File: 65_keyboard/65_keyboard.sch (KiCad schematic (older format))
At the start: 10 parts, among them SW0-0 MX, SW1-0 MX, SW2-0 MX, SW3-0 MX, SW4-0 MX

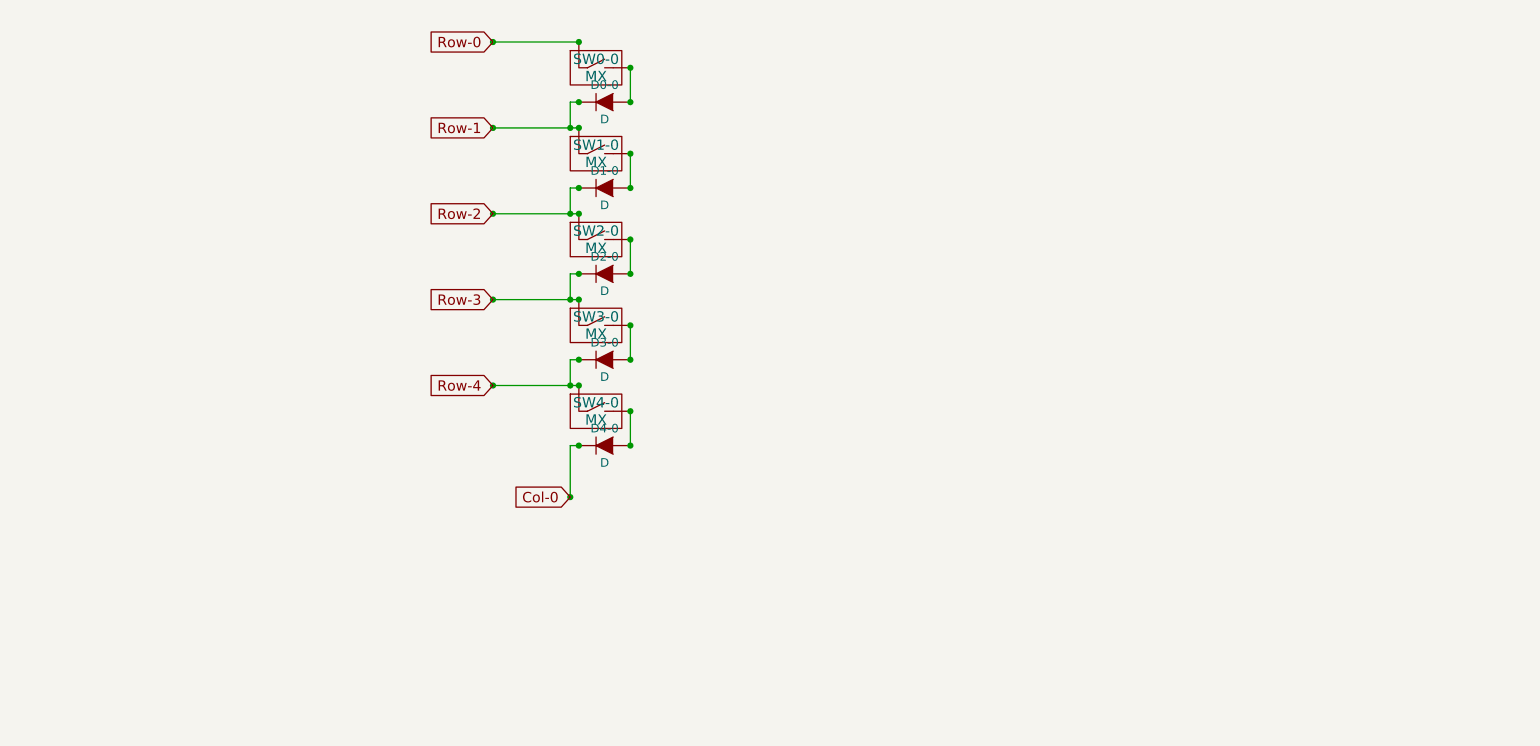
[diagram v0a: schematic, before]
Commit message: Adds all keys to keyboard, and places them on the PCB
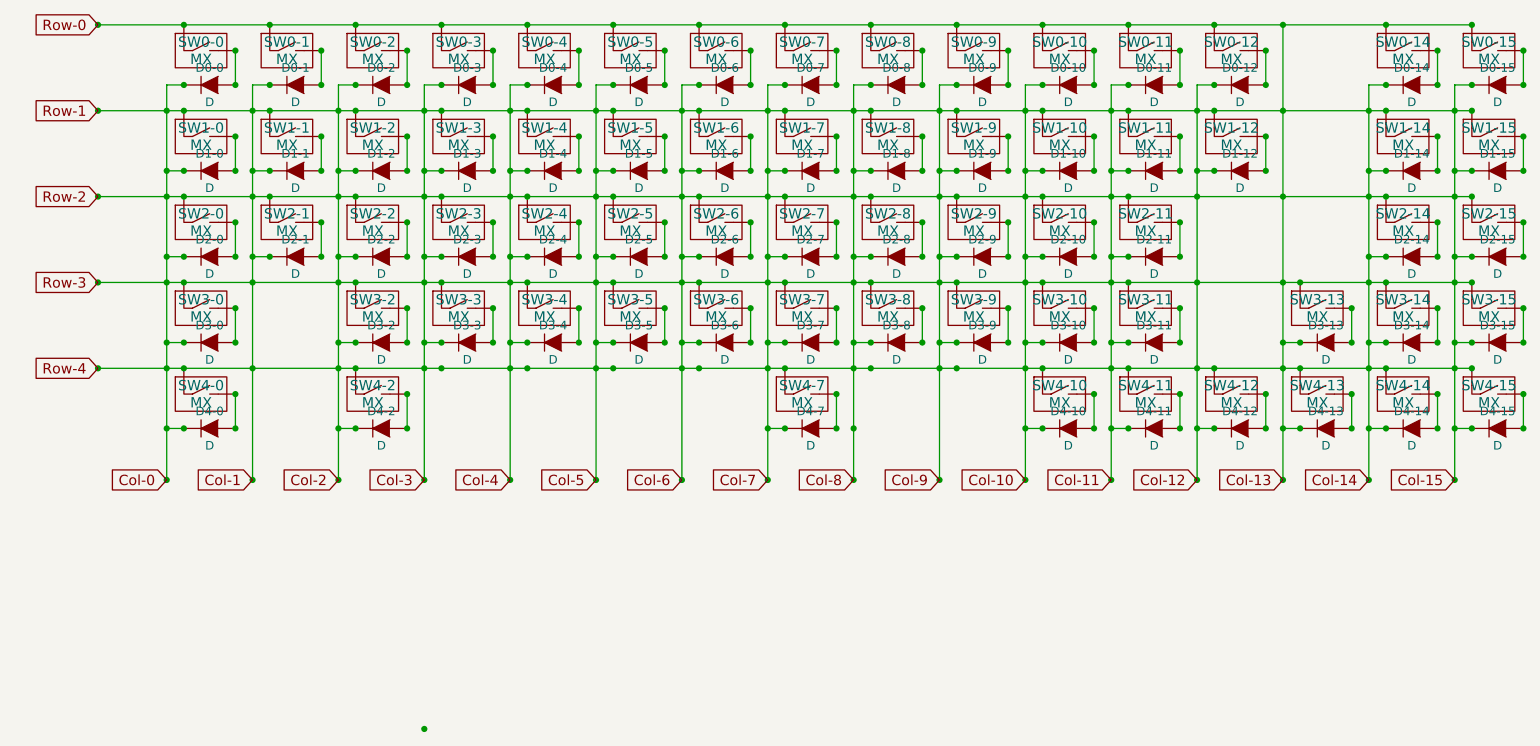
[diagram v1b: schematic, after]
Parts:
- added D0-1, D0-10, D0-11, D0-12, D0-14, D0-15, D0-2, D0-3, D0-4, D0-5, D0-6, D0-7, D0-8, D0-9, D1-1, D1-10, D1-11, D1-12, D1-14, D1-15, D1-2, D1-3, D1-4, D1-5, D1-6, D1-7, D1-8, D1-9, D2-1, D2-10, D2-11, D2-14, D2-15, D2-2, D2-3, D2-4, D2-5, D2-6, D2-7, D2-8, D2-9, D3-10, D3-11, D3-13, D3-14, D3-15, D3-2, D3-3, D3-4, D3-5, D3-6, D3-7, D3-8, D3-9, D4-10, D4-11, D4-12, D4-13, D4-14, D4-15, D4-2, D4-7: D, Diodes_ThroughHole:Diode_DO-35_SOD27_Horizontal_RM10, symbol D
- added SW0-1, SW0-10, SW0-11, SW0-12, SW0-15, SW0-2, SW0-3, SW0-4, SW0-5, SW0-6, SW0-7, SW0-8, SW0-9, SW1-1, SW1-10, SW1-11, SW1-12, SW1-15, SW1-2, SW1-3, SW1-4, SW1-5, SW1-6, SW1-7, SW1-8, SW1-9, SW2-1, SW2-10, SW2-11, SW2-15, SW2-2, SW2-3, SW2-4, SW2-5, SW2-6, SW2-7, SW2-8, SW2-9, SW3-10, SW3-11, SW3-14, SW3-15, SW3-2, SW3-3, SW3-4, SW3-5, SW3-6, SW3-7, SW3-8, SW3-9, SW4-11, SW4-13, SW4-14, SW4-15: MX, Keyboard:CHERRY_PLATE_100H, symbol MX
- added SW0-14: MX, Keyboard:CHERRY_PLATE_200H, symbol MX
- added SW1-14, SW4-2: MX, Keyboard:CHERRY_PLATE_150H, symbol MX
- added SW2-14: MX, Keyboard:CHERRY_PLATE_225H, symbol MX
- added SW3-13: MX, Keyboard:CHERRY_PLATE_175H, symbol MX
- added SW4-10, SW4-12: MX, Keyboard:CHERRY_PLATE_125H, symbol MX
- added SW4-7: MX, Keyboard:CHERRY_PLATE_625H, symbol MX
- SW0-0: footprint Keyboard:CHERRY_PCB_100H -> Keyboard:CHERRY_PLATE_100H
- SW1-0: footprint Keyboard:CHERRY_PCB_150H -> Keyboard:CHERRY_PLATE_150H
- SW2-0: footprint Keyboard:CHERRY_PCB_200H -> Keyboard:CHERRY_PLATE_175H
- SW3-0: footprint Keyboard:CHERRY_PCB_275H -> Keyboard:CHERRY_PLATE_225H
- SW4-0: footprint Keyboard:CHERRY_PLATE_150H -> Keyboard:CHERRY_PLATE_175H
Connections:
- net Row-0 is gone; now on net Col-0: SW0-0.1 (A)
- net Row-1 is gone; now on net Col-0: D0-0.1 (K), SW1-0.1 (A)
- net Row-2 is gone; now on net Col-0: D1-0.1 (K), SW2-0.1 (A)
- net Row-3 is gone; now on net Col-0: D2-0.1 (K), SW3-0.1 (A)
- net Row-4 is gone; now on net Col-0: D3-0.1 (K), SW4-0.1 (A)
- net Col-0: now also D0-1.1 (K), D0-10.1 (K), D0-11.1 (K), D0-12.1 (K), D0-14.1 (K), D0-15.1 (K), D0-2.1 (K), D0-3.1 (K), D0-4.1 (K), D0-5.1 (K), D0-6.1 (K), D0-7.1 (K), D0-8.1 (K), D0-9.1 (K), D1-1.1 (K), D1-10.1 (K), D1-11.1 (K), D1-12.1 (K), D1-14.1 (K), D1-15.1 (K), D1-2.1 (K), D1-3.1 (K), D1-4.1 (K), D1-5.1 (K), D1-6.1 (K), D1-7.1 (K), D1-8.1 (K), D1-9.1 (K), D2-1.1 (K), D2-10.1 (K), D2-11.1 (K), D2-14.1 (K), D2-15.1 (K), D2-2.1 (K), D2-3.1 (K), D2-4.1 (K), D2-5.1 (K), D2-6.1 (K), D2-7.1 (K), D2-8.1 (K), D2-9.1 (K), D3-10.1 (K), D3-11.1 (K), D3-13.1 (K), D3-14.1 (K), D3-15.1 (K), D3-2.1 (K), D3-3.1 (K), D3-4.1 (K), D3-5.1 (K), D3-6.1 (K), D3-7.1 (K), D3-8.1 (K), D3-9.1 (K), D4-10.1 (K), D4-11.1 (K), D4-12.1 (K), D4-13.1 (K), D4-14.1 (K), D4-15.1 (K), D4-2.1 (K), D4-7.1 (K), SW0-1.1 (A), SW0-10.1 (A), SW0-11.1 (A), SW0-12.1 (A), SW0-14.1 (A), SW0-15.1 (A), SW0-2.1 (A), SW0-3.1 (A), SW0-4.1 (A), SW0-5.1 (A), SW0-6.1 (A), SW0-7.1 (A), SW0-8.1 (A), SW0-9.1 (A), SW1-1.1 (A), SW1-10.1 (A), SW1-11.1 (A), SW1-12.1 (A), SW1-14.1 (A), SW1-15.1 (A), SW1-2.1 (A), SW1-3.1 (A), SW1-4.1 (A), SW1-5.1 (A), SW1-6.1 (A), SW1-7.1 (A), SW1-8.1 (A), SW1-9.1 (A), SW2-1.1 (A), SW2-10.1 (A), SW2-11.1 (A), SW2-14.1 (A), SW2-15.1 (A), SW2-2.1 (A), SW2-3.1 (A), SW2-4.1 (A), SW2-5.1 (A), SW2-6.1 (A), SW2-7.1 (A), SW2-8.1 (A), SW2-9.1 (A), SW3-10.1 (A), SW3-11.1 (A), SW3-13.1 (A), SW3-14.1 (A), SW3-15.1 (A), SW3-2.1 (A), SW3-3.1 (A), SW3-4.1 (A), SW3-5.1 (A), SW3-6.1 (A), SW3-7.1 (A), SW3-8.1 (A), SW3-9.1 (A), SW4-10.1 (A), SW4-11.1 (A), SW4-12.1 (A), SW4-13.1 (A), SW4-14.1 (A), SW4-15.1 (A), SW4-2.1 (A), SW4-7.1 (A)
- new net: D0-1.2 (A), SW0-1.2 (B)
- new net: D1-1.2 (A), SW1-1.2 (B)
- new net: D2-1.2 (A), SW2-1.2 (B)
- new net: D0-2.2 (A), SW0-2.2 (B)
- new net: D1-2.2 (A), SW1-2.2 (B)
- new net: D2-2.2 (A), SW2-2.2 (B)
- new net: D3-2.2 (A), SW3-2.2 (B)
- new net: D4-2.2 (A), SW4-2.2 (B)
- new net: D0-3.2 (A), SW0-3.2 (B)
- new net: D1-3.2 (A), SW1-3.2 (B)
- new net: D2-3.2 (A), SW2-3.2 (B)
- new net: D3-3.2 (A), SW3-3.2 (B)
- new net: D0-4.2 (A), SW0-4.2 (B)
- new net: D1-4.2 (A), SW1-4.2 (B)
- new net: D2-4.2 (A), SW2-4.2 (B)
- new net: D3-4.2 (A), SW3-4.2 (B)
- new net: D0-5.2 (A), SW0-5.2 (B)
- new net: D1-5.2 (A), SW1-5.2 (B)
- new net: D2-5.2 (A), SW2-5.2 (B)
- new net: D3-5.2 (A), SW3-5.2 (B)
- new net: D0-6.2 (A), SW0-6.2 (B)
- new net: D1-6.2 (A), SW1-6.2 (B)
- new net: D2-6.2 (A), SW2-6.2 (B)
- new net: D3-6.2 (A), SW3-6.2 (B)
- new net: D0-7.2 (A), SW0-7.2 (B)
- new net: D1-7.2 (A), SW1-7.2 (B)
- new net: D2-7.2 (A), SW2-7.2 (B)
- new net: D3-7.2 (A), SW3-7.2 (B)
- new net: D4-7.2 (A), SW4-7.2 (B)
- new net: D0-8.2 (A), SW0-8.2 (B)
- new net: D1-8.2 (A), SW1-8.2 (B)
- new net: D2-8.2 (A), SW2-8.2 (B)
- new net: D3-8.2 (A), SW3-8.2 (B)
- new net: D0-9.2 (A), SW0-9.2 (B)
- new net: D1-9.2 (A), SW1-9.2 (B)
- new net: D2-9.2 (A), SW2-9.2 (B)
- new net: D3-9.2 (A), SW3-9.2 (B)
- new net: D0-10.2 (A), SW0-10.2 (B)
- new net: D1-10.2 (A), SW1-10.2 (B)
- new net: D2-10.2 (A), SW2-10.2 (B)
- new net: D3-10.2 (A), SW3-10.2 (B)
- new net: D4-10.2 (A), SW4-10.2 (B)
- new net: D0-11.2 (A), SW0-11.2 (B)
- new net: D1-11.2 (A), SW1-11.2 (B)
- new net: D2-11.2 (A), SW2-11.2 (B)
- new net: D3-11.2 (A), SW3-11.2 (B)
- new net: D4-11.2 (A), SW4-11.2 (B)
- new net: D0-12.2 (A), SW0-12.2 (B)
- new net: D1-12.2 (A), SW1-12.2 (B)
- new net: D4-12.2 (A), SW4-12.2 (B)
- new net: D3-13.2 (A), SW3-13.2 (B)
- new net: D4-13.2 (A), SW4-13.2 (B)
- new net: D0-14.2 (A), SW0-14.2 (B)
- new net: D1-14.2 (A), SW1-14.2 (B)
- new net: D2-14.2 (A), SW2-14.2 (B)
- new net: D3-14.2 (A), SW3-14.2 (B)
- new net: D4-14.2 (A), SW4-14.2 (B)
- new net: D0-15.2 (A), SW0-15.2 (B)
- new net: D1-15.2 (A), SW1-15.2 (B)
- new net: D2-15.2 (A), SW2-15.2 (B)
- new net: D3-15.2 (A), SW3-15.2 (B)
- new net: D4-15.2 (A), SW4-15.2 (B)
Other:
- moved on the sheet: D0-0, D1-0, D2-0, D3-0, D4-0, SW0-0, SW1-0, SW2-0, SW3-0, SW4-0

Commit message: Removes useless junctions
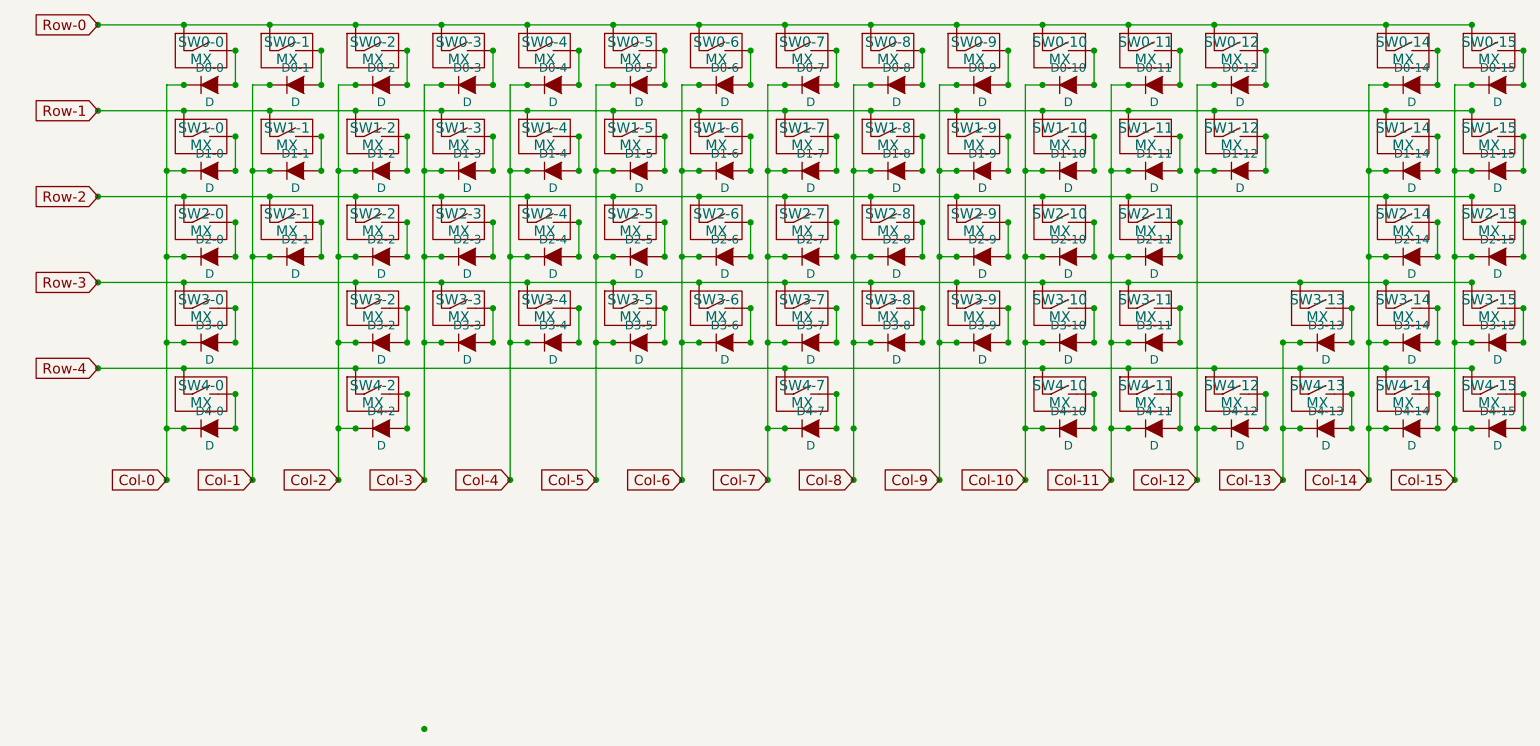
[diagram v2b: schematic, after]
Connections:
- net Col-0: no longer D0-1.1 (K), D0-10.1 (K), D0-11.1 (K), D0-12.1 (K), D0-14.1 (K), D0-15.1 (K), D0-2.1 (K), D0-3.1 (K), D0-4.1 (K), D0-5.1 (K), D0-6.1 (K), D0-7.1 (K), D0-8.1 (K), D0-9.1 (K), D1-1.1 (K), D1-10.1 (K), D1-11.1 (K), D1-12.1 (K), D1-14.1 (K), D1-15.1 (K), D1-2.1 (K), D1-3.1 (K), D1-4.1 (K), D1-5.1 (K), D1-6.1 (K), D1-7.1 (K), D1-8.1 (K), D1-9.1 (K), D2-1.1 (K), D2-10.1 (K), D2-11.1 (K), D2-14.1 (K), D2-15.1 (K), D2-2.1 (K), D2-3.1 (K), D2-4.1 (K), D2-5.1 (K), D2-6.1 (K), D2-7.1 (K), D2-8.1 (K), D2-9.1 (K), D3-10.1 (K), D3-11.1 (K), D3-13.1 (K), D3-14.1 (K), D3-15.1 (K), D3-2.1 (K), D3-3.1 (K), D3-4.1 (K), D3-5.1 (K), D3-6.1 (K), D3-7.1 (K), D3-8.1 (K), D3-9.1 (K), D4-10.1 (K), D4-11.1 (K), D4-12.1 (K), D4-13.1 (K), D4-14.1 (K), D4-15.1 (K), D4-2.1 (K), D4-7.1 (K), SW0-0.1 (A), SW0-1.1 (A), SW0-10.1 (A), SW0-11.1 (A), SW0-12.1 (A), SW0-14.1 (A), SW0-15.1 (A), SW0-2.1 (A), SW0-3.1 (A), SW0-4.1 (A), SW0-5.1 (A), SW0-6.1 (A), SW0-7.1 (A), SW0-8.1 (A), SW0-9.1 (A), SW1-0.1 (A), SW1-1.1 (A), SW1-10.1 (A), SW1-11.1 (A), SW1-12.1 (A), SW1-14.1 (A), SW1-15.1 (A), SW1-2.1 (A), SW1-3.1 (A), SW1-4.1 (A), SW1-5.1 (A), SW1-6.1 (A), SW1-7.1 (A), SW1-8.1 (A), SW1-9.1 (A), SW2-0.1 (A), SW2-1.1 (A), SW2-10.1 (A), SW2-11.1 (A), SW2-14.1 (A), SW2-15.1 (A), SW2-2.1 (A), SW2-3.1 (A), SW2-4.1 (A), SW2-5.1 (A), SW2-6.1 (A), SW2-7.1 (A), SW2-8.1 (A), SW2-9.1 (A), SW3-0.1 (A), SW3-10.1 (A), SW3-11.1 (A), SW3-13.1 (A), SW3-14.1 (A), SW3-15.1 (A), SW3-2.1 (A), SW3-3.1 (A), SW3-4.1 (A), SW3-5.1 (A), SW3-6.1 (A), SW3-7.1 (A), SW3-8.1 (A), SW3-9.1 (A), SW4-0.1 (A), SW4-10.1 (A), SW4-11.1 (A), SW4-12.1 (A), SW4-13.1 (A), SW4-14.1 (A), SW4-15.1 (A), SW4-2.1 (A), SW4-7.1 (A)
- new net Col-1: D0-1.1 (K), D1-1.1 (K), D2-1.1 (K)
- new net Col-10: D0-10.1 (K), D1-10.1 (K), D2-10.1 (K), D3-10.1 (K), D4-10.1 (K)
- new net Col-11: D0-11.1 (K), D1-11.1 (K), D2-11.1 (K), D3-11.1 (K), D4-11.1 (K)
- new net Col-12: D0-12.1 (K), D1-12.1 (K), D4-12.1 (K)
- new net Col-13: D3-13.1 (K), D4-13.1 (K)
- new net Col-14: D0-14.1 (K), D1-14.1 (K), D2-14.1 (K), D3-14.1 (K), D4-14.1 (K)
- new net Col-15: D0-15.1 (K), D1-15.1 (K), D2-15.1 (K), D3-15.1 (K), D4-15.1 (K)
- new net Col-2: D0-2.1 (K), D1-2.1 (K), D2-2.1 (K), D3-2.1 (K), D4-2.1 (K)
- new net Col-3: D0-3.1 (K), D1-3.1 (K), D2-3.1 (K), D3-3.1 (K)
- new net Col-4: D0-4.1 (K), D1-4.1 (K), D2-4.1 (K), D3-4.1 (K)
- new net Col-5: D0-5.1 (K), D1-5.1 (K), D2-5.1 (K), D3-5.1 (K)
- new net Col-6: D0-6.1 (K), D1-6.1 (K), D2-6.1 (K), D3-6.1 (K)
- new net Col-7: D0-7.1 (K), D1-7.1 (K), D2-7.1 (K), D3-7.1 (K), D4-7.1 (K)
- new net Col-8: D0-8.1 (K), D1-8.1 (K), D2-8.1 (K), D3-8.1 (K)
- new net Col-9: D0-9.1 (K), D1-9.1 (K), D2-9.1 (K), D3-9.1 (K)
- new net Row-0: SW0-0.1 (A), SW0-1.1 (A), SW0-10.1 (A), SW0-11.1 (A), SW0-12.1 (A), SW0-14.1 (A), SW0-15.1 (A), SW0-2.1 (A), SW0-3.1 (A), SW0-4.1 (A), SW0-5.1 (A), SW0-6.1 (A), SW0-7.1 (A), SW0-8.1 (A), SW0-9.1 (A)
- new net Row-1: SW1-0.1 (A), SW1-1.1 (A), SW1-10.1 (A), SW1-11.1 (A), SW1-12.1 (A), SW1-14.1 (A), SW1-15.1 (A), SW1-2.1 (A), SW1-3.1 (A), SW1-4.1 (A), SW1-5.1 (A), SW1-6.1 (A), SW1-7.1 (A), SW1-8.1 (A), SW1-9.1 (A)
- new net Row-2: SW2-0.1 (A), SW2-1.1 (A), SW2-10.1 (A), SW2-11.1 (A), SW2-14.1 (A), SW2-15.1 (A), SW2-2.1 (A), SW2-3.1 (A), SW2-4.1 (A), SW2-5.1 (A), SW2-6.1 (A), SW2-7.1 (A), SW2-8.1 (A), SW2-9.1 (A)
- new net Row-3: SW3-0.1 (A), SW3-10.1 (A), SW3-11.1 (A), SW3-13.1 (A), SW3-14.1 (A), SW3-15.1 (A), SW3-2.1 (A), SW3-3.1 (A), SW3-4.1 (A), SW3-5.1 (A), SW3-6.1 (A), SW3-7.1 (A), SW3-8.1 (A), SW3-9.1 (A)
- new net Row-4: SW4-0.1 (A), SW4-10.1 (A), SW4-11.1 (A), SW4-12.1 (A), SW4-13.1 (A), SW4-14.1 (A), SW4-15.1 (A), SW4-2.1 (A), SW4-7.1 (A)
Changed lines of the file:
@@
 $EndComp
 Connection ~ 1800 2550
-Connection ~ 1500 2550
 Wire Wire Line
 	1400 2550 1500 2550
@@
 Connection ~ 1500 1200
 Connection ~ 1000 1200
-Connection ~ 1400 1200
 Connection ~ 1400 3350
 Connection ~ 1400 3050
@@
 	1500 1550 1400 1550
 Connection ~ 1400 1550
-Connection ~ 1400 2700
-Connection ~ 1400 2200
-Connection ~ 1400 1700
 Connection ~ 1400 2050
 Connection ~ 1500 1700
@@
 Col-1
 Connection ~ 2000 1200
-Connection ~ 1900 1200
 Connection ~ 1900 3350
 Wire Wire Line
 	2000 1550 1900 1550
 Connection ~ 1900 1550
-Connection ~ 1900 2700
-Connection ~ 1900 2200
-Connection ~ 1900 1700
 Connection ~ 1900 2050
 Connection ~ 2000 1700
@@
 $EndComp
 Connection ~ 2800 2550
-Connection ~ 2500 2550
 Wire Wire Line
 	2400 2550 2500 2550
@@
 Col-2
 Connection ~ 2500 1200
-Connection ~ 2400 1200
 Connection ~ 2400 3350
 Connection ~ 2400 3050
@@
 	2500 1550 2400 1550
 Connection ~ 2400 1550
-Connection ~ 2400 2700
-Connection ~ 2400 2200
-Connection ~ 2400 1700
 Connection ~ 2400 2050
 Connection ~ 2500 1700
@@
 Wire Wire Line
 	2900 2550 3000 2550
-Connection ~ 3000 2700
 Text GLabel 2900 3350 0    60   Input ~ 0
 Col-3
 Connection ~ 3000 1200
-Connection ~ 2900 1200
 Connection ~ 2900 3350
 Connection ~ 2900 2550
@@
 	3000 1550 2900 1550
 Connection ~ 2900 1550
-Connection ~ 2900 2700
-Connection ~ 2900 2200
-Connection ~ 2900 1700
 Connection ~ 2900 2050
 Connection ~ 3000 1700
@@
 Wire Wire Line
 	3400 2550 3500 2550
-Connection ~ 3500 2700
 Text GLabel 3400 3350 0    60   Input ~ 0
 Col-4
 Connection ~ 3500 1200
-Connection ~ 3400 1200
 Connection ~ 3400 3350
 Connection ~ 3400 2550
@@
 	3500 1550 3400 1550
 Connection ~ 3400 1550
-Connection ~ 3400 2700
-Connection ~ 3400 2200
-Connection ~ 3400 1700
 Connection ~ 3400 2050
 Connection ~ 3500 1700
@@
 Wire Wire Line
 	3900 2550 4000 2550
-Connection ~ 4000 2700
 Text GLabel 3900 3350 0    60   Input ~ 0
 Col-5
 Connection ~ 4000 1200
-Connection ~ 3900 1200
 Connection ~ 3900 3350
 Connection ~ 3900 2550
@@
 	4000 1550 3900 1550
 Connection ~ 3900 1550
-Connection ~ 3900 2700
-Connection ~ 3900 2200
-Connection ~ 3900 1700
 Connection ~ 3900 2050
 Connection ~ 4000 1700
@@
 Wire Wire Line
 	4400 2550 4500 2550
-Connection ~ 4500 2700
 Text GLabel 4400 3350 0    60   Input ~ 0
 Col-6
 Connection ~ 4500 1200
-Connection ~ 4400 1200
 Connection ~ 4400 3350
 Connection ~ 4400 2550
@@
 	4500 1550 4400 1550
 Connection ~ 4400 1550
-Connection ~ 4400 2700
-Connection ~ 4400 2200
-Connection ~ 4400 1700
 Connection ~ 4400 2050
 Connection ~ 4500 1700
@@
 Col-7
 Connection ~ 5000 1200
-Connection ~ 4900 1200
 Connection ~ 4900 3350
 Connection ~ 4900 3050
@@
 	5000 1550 4900 1550
 Connection ~ 4900 1550
-Connection ~ 4900 2700
-Connection ~ 4900 2200
-Connection ~ 4900 1700
 Connection ~ 4900 2050
 Connection ~ 5000 1700
@@
 Wire Wire Line
 	5400 2550 5500 2550
-Connection ~ 5500 2700
 Text GLabel 5400 3350 0    60   Input ~ 0
 Col-8
 Connection ~ 5500 1200
-Connection ~ 5400 1200
 Connection ~ 5400 3350
 Connection ~ 5400 3050
@@
 	5500 1550 5400 1550
 Connection ~ 5400 1550
-Connection ~ 5400 2700
-Connection ~ 5400 2200
-Connection ~ 5400 1700
 Connection ~ 5400 2050
 Connection ~ 5500 1700
@@
 Wire Wire Line
 	5900 2550 6000 2550
-Connection ~ 6000 2700
 Text GLabel 5900 3350 0    60   Input ~ 0
 Col-9
 Connection ~ 6000 1200
-Connection ~ 5900 1200
 Connection ~ 5900 3350
 Connection ~ 5900 2550
@@
 	6000 1550 5900 1550
 Connection ~ 5900 1550
-Connection ~ 5900 2700
-Connection ~ 5900 2200
-Connection ~ 5900 1700
 Connection ~ 5900 2050
 Connection ~ 6000 1700
@@
 Col-10
 Connection ~ 6500 1200
-Connection ~ 6400 1200
 Connection ~ 6400 3350
 Connection ~ 6400 3050
@@
 	6500 1550 6400 1550
 Connection ~ 6400 1550
-Connection ~ 6400 2700
-Connection ~ 6400 2200
-Connection ~ 6400 1700
 Connection ~ 6400 2050
 Connection ~ 6500 1700
@@
 Col-11
 Connection ~ 7000 1200
-Connection ~ 6900 1200
 Connection ~ 6900 3350
 Connection ~ 6900 3050
@@
 	7000 1550 6900 1550
 Connection ~ 6900 1550
-Connection ~ 6900 2700
-Connection ~ 6900 2200
-Connection ~ 6900 1700
 Connection ~ 6900 2050
 Connection ~ 7000 1700
@@
 Col-12
 Connection ~ 7500 1200
-Connection ~ 7400 1200
 Connection ~ 7400 3350
 Connection ~ 7400 3050
@@
 	7500 1550 7400 1550
 Connection ~ 7400 1550
-Connection ~ 7400 2700
-Connection ~ 7400 2200
-Connection ~ 7400 1700
 $Comp
 L MX SW3-13
@@
 Connection ~ 8000 3050
 Connection ~ 7900 2550
-Connection ~ 7900 2700
 $Comp
 L MX SW0-14
@@
 Col-14
 Connection ~ 8500 1200
-Connection ~ 8400 1200
 Connection ~ 8400 3350
 Connection ~ 8400 3050
@@
 	8500 1550 8400 1550
 Connection ~ 8400 1550
-Connection ~ 8400 2700
-Connection ~ 8400 2200
-Connection ~ 8400 1700
 Connection ~ 8400 2050
 Connection ~ 8500 1700
@@
 Col-15
 Connection ~ 9000 1200
-Connection ~ 8900 1200
 Connection ~ 8900 3350
 Connection ~ 8900 3050
@@
 	9000 1550 8900 1550
 Connection ~ 8900 1550
-Connection ~ 8900 2700
-Connection ~ 8900 2200
-Connection ~ 8900 1700
 Connection ~ 8900 2050
 Connection ~ 9000 1700
 Wire Wire Line
-	7900 700  7900 3350
-Connection ~ 7900 700
-Connection ~ 7900 1200
-Connection ~ 7900 1700
-Wire Wire Line
 	1000 2200 9000 2200
-Connection ~ 7900 2200
 Connection ~ 2900 4800
+Connection ~ 1500 2550
+Connection ~ 2500 2550
+Wire Wire Line
+	7900 2550 7900 3350
 $EndSCHEMATC
